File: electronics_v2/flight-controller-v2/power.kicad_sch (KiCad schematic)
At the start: 39 parts, among them J1 Conn_01x02, J2 Conn_01x03, J3 Conn_01x03, J4 Conn_01x03, J5 Conn_01x03, J6 Conn_01x03, J7 Conn_01x02, Q1 IRFR5305, SW1 SW_Push_SPDT, U1 LM1117-3.3, U2 MP1584, U3 INA226

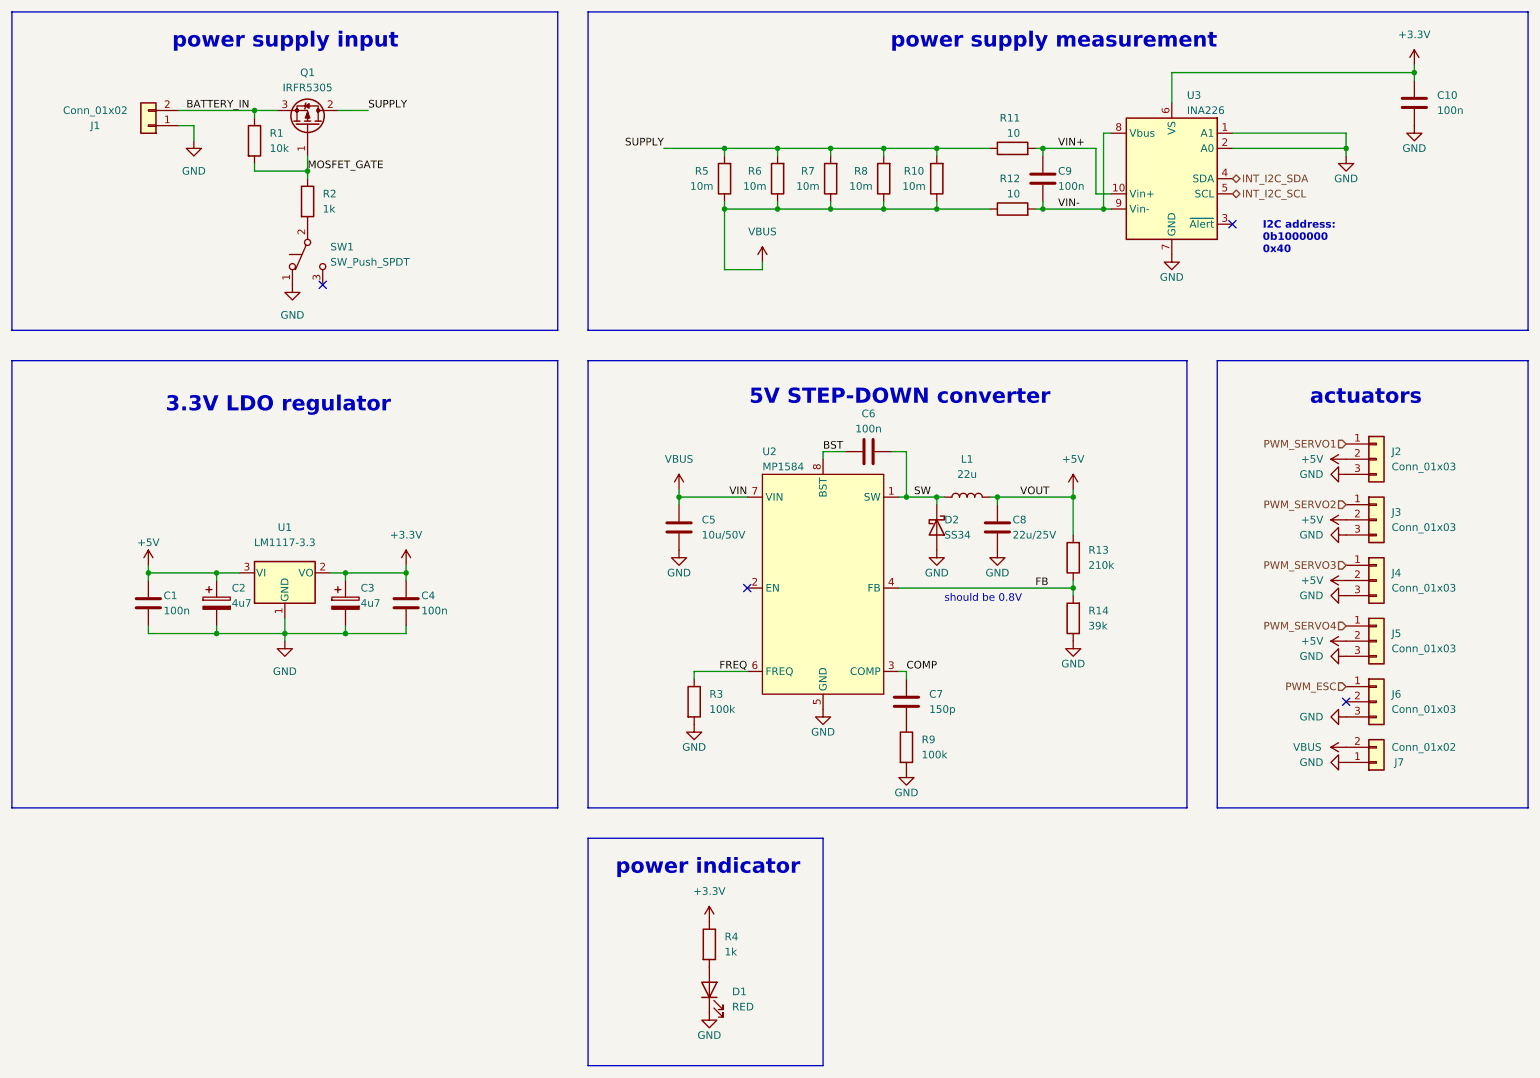
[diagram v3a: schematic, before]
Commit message: fix route names
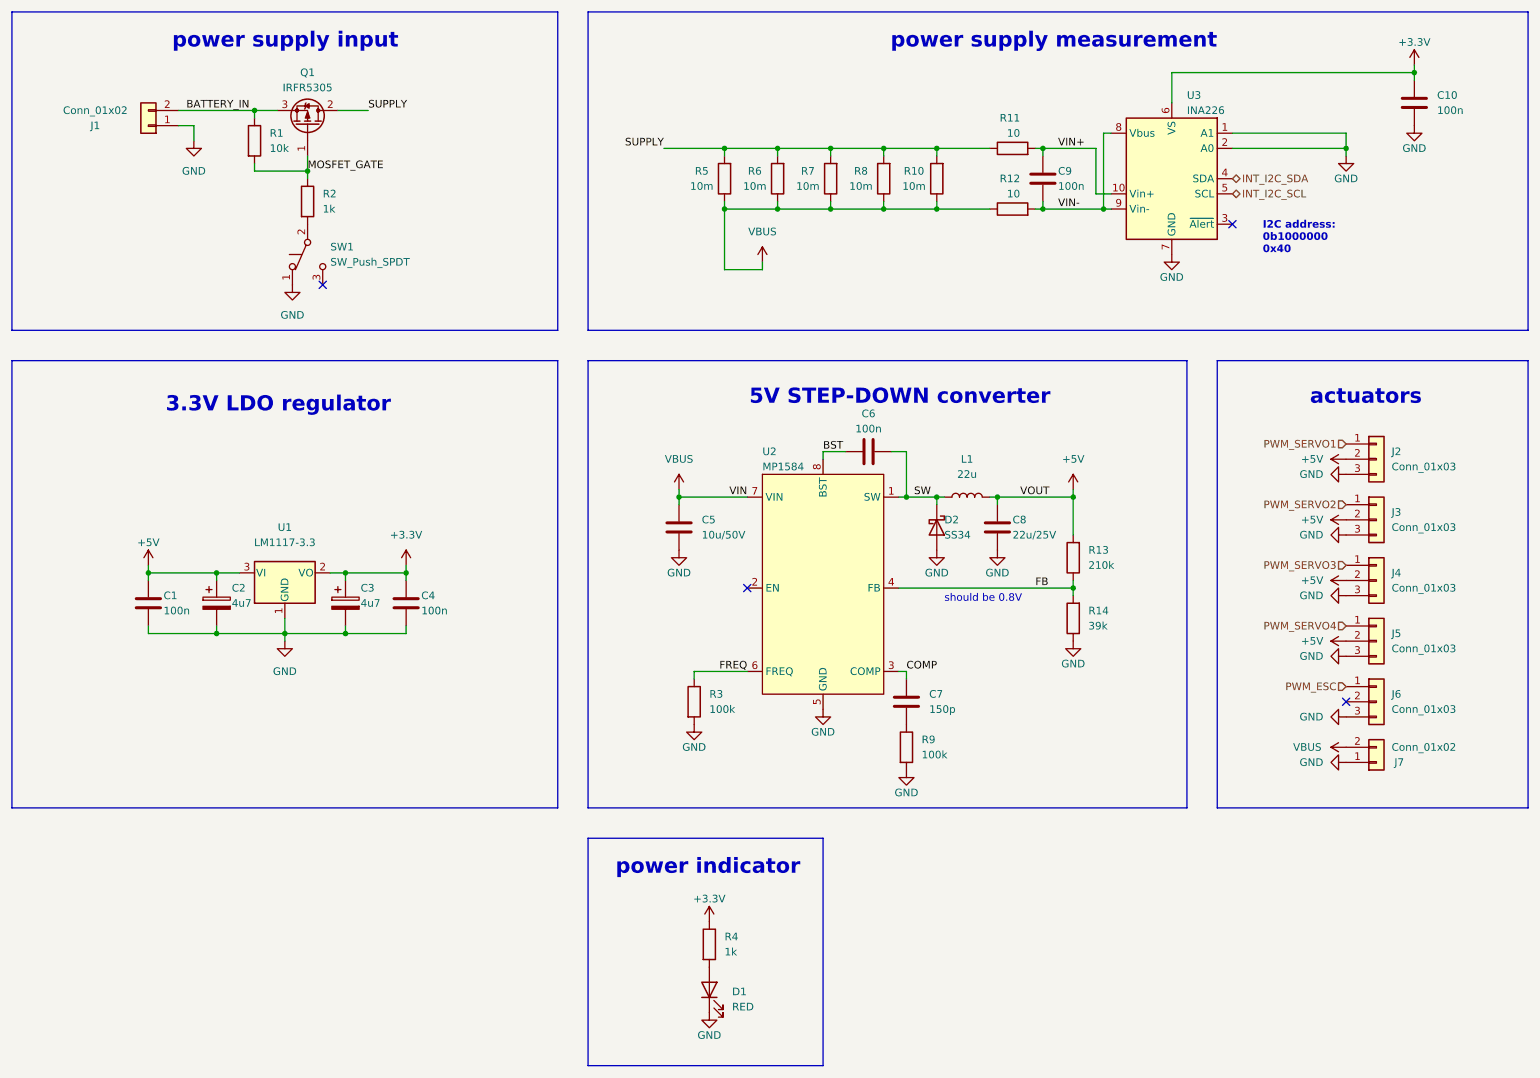
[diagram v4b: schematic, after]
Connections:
- net +3V3 is gone; now on net +3.3V: C10.2, R4.1, U3.6 (VS)
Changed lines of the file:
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@@
     (pin "2")
+  )
+  (symbol (lib_id "power:+3.3V") (at 133.35 168.91 0) (unit 1)
+    (in_bom yes) (on_board yes)
+    (property "Reference" "#PWR?" (id 0) (at 133.35 172.72 0)
+      (effects (font (size 1.27 1.27)) hide)
+    )
+    (property "Value" "+3.3V" (id 1) (at 133.35 165.1 0))
+    (property "Footprint" "" (id 2) (at 133.35 168.91 0)
+      (effects (font (size 1.27 1.27)) hide)
+    )
+    (property "Datasheet" "" (id 3) (at 133.35 168.91 0)
+      (effects (font (size 1.27 1.27)) hide)
+    )
+    (pin "1")
   )
   (symbol (lib_id "power:GND") (at 240.03 40.64 0) (unit 1)
@@
     (pin "1")
     (pin "2")
-  )
-  (symbol (lib_name "+3.3V_1") (lib_id "power:+3.3V") (at 133.35 168.91 0) (unit 1)
-    (in_bom yes) (on_board yes) (fields_autoplaced)
-    (property "Reference" "#PWR010" (id 0) (at 133.35 172.72 0)
-      (effects (font (size 1.27 1.27)) hide)
-    )
-    (property "Value" "+3.3V" (id 1) (at 133.35 163.83 0))
-    (property "Footprint" "" (id 2) (at 133.35 168.91 0)
-      (effects (font (size 1.27 1.27)) hide)
-    )
-    (property "Datasheet" "" (id 3) (at 133.35 168.91 0)
-      (effects (font (size 1.27 1.27)) hide)
-    )
-    (pin "1")
   )
   (symbol (lib_id "Device:C") (at 166.37 132.08 0) (unit 1)
@@
     (pin "1")
   )
+  (symbol (lib_id "power:+3.3V") (at 251.46 25.4 0) (unit 1)
+    (in_bom yes) (on_board yes)
+    (property "Reference" "#PWR0106" (id 0) (at 251.46 29.21 0)
+      (effects (font (size 1.27 1.27)) hide)
+    )
+    (property "Value" "+3.3V" (id 1) (at 251.46 21.59 0))
+    (property "Footprint" "" (id 2) (at 251.46 25.4 0)
+      (effects (font (size 1.27 1.27)) hide)
+    )
+    (property "Datasheet" "" (id 3) (at 251.46 25.4 0)
+      (effects (font (size 1.27 1.27)) hide)
+    )
+    (pin "1")
+  )
   (symbol (lib_id "Device:R") (at 184.15 49.53 90) (unit 1)
     (in_bom yes) (on_board yes)
@@
       (effects (font (size 1.27 1.27)) hide)
     )
-    (pin "1")
-  )
-  (symbol (lib_name "+3.3V_1") (lib_id "power:+3.3V") (at 251.46 25.4 0) (unit 1)
-    (in_bom yes) (on_board yes) (fields_autoplaced)
-    (property "Reference" "#PWR032" (id 0) (at 251.46 29.21 0)
-      (effects (font (size 1.27 1.27)) hide)
-    )
-    (property "Value" "+3.3V" (id 1) (at 251.46 20.32 0))
-    (property "Footprint" "" (id 2) (at 251.46 25.4 0)
-      (effects (font (size 1.27 1.27)) hide)
-    )
-    (property "Datasheet" "" (id 3) (at 251.46 25.4 0)
-      (effects (font (size 1.27 1.27)) hide)
-    )

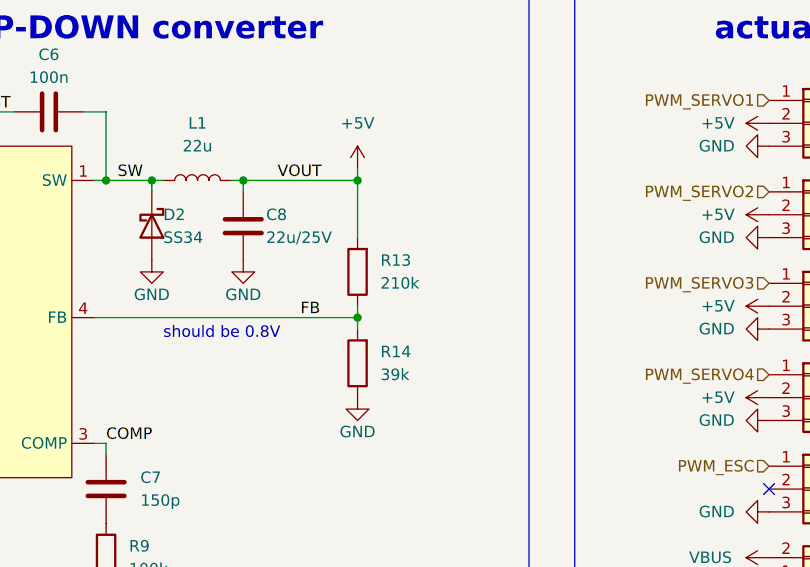
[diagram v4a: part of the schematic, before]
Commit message: fix gitignore and find more fitting resistor
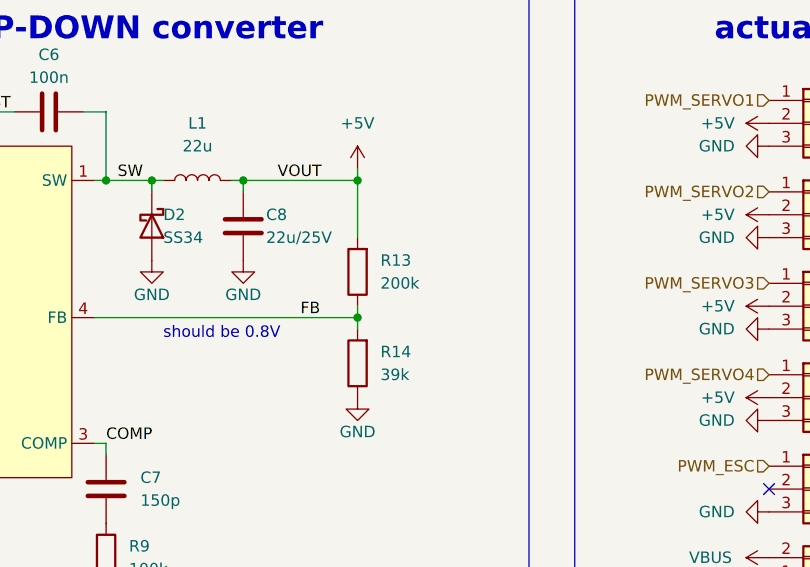
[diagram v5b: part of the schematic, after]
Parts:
- R13: value 210k -> 200k
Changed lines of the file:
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@@
   (symbol (lib_id "power:+3.3V") (at 133.35 168.91 0) (unit 1)
     (in_bom yes) (on_board yes)
-    (property "Reference" "#PWR?" (id 0) (at 133.35 172.72 0)
+    (property "Reference" "#PWR0107" (id 0) (at 133.35 172.72 0)
       (effects (font (size 1.27 1.27)) hide)
     )
@@
       (effects (font (size 1.27 1.27)) (justify right))
     )
-    (property "Value" "210k" (id 1) (at 196.85 109.2199 0)
-      (effects (font (size 1.27 1.27)) (justify right))
-    )
+    (property "Value" "200k" (id 1) (at 196.85 109.2199 0)
+      (effects (font (size 1.27 1.27)) (justify right))
+    )

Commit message: route new FC
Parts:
- D1: value RED -> LED
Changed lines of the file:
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@@
   (symbol (lib_id "power:+3.3V") (at 133.35 168.91 0) (unit 1)
     (in_bom yes) (on_board yes)
-    (property "Reference" "#PWR0107" (id 0) (at 133.35 172.72 0)
+    (property "Reference" "#PWR010" (id 0) (at 133.35 172.72 0)
       (effects (font (size 1.27 1.27)) hide)
     )
@@
       (effects (font (size 1.27 1.27)) (justify right))
     )
-    (property "Value" "RED" (id 1) (at 137.16 183.1974 90)
+    (property "Value" "LED" (id 1) (at 137.16 183.1974 90)
       (effects (font (size 1.27 1.27)) (justify right))
     )
@@
   (symbol (lib_id "power:+3.3V") (at 251.46 25.4 0) (unit 1)
     (in_bom yes) (on_board yes)
-    (property "Reference" "#PWR0106" (id 0) (at 251.46 29.21 0)
-      (effects (font (size 1.27 1.27)) hide)
-    )
+    (property "Reference" "#PWR032" (id 0) (at 251.46 29.21 0)
+      (effects (font (size 1.27 1.27)) hide)
+    )
